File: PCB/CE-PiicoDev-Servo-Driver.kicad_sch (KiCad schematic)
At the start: 33 parts, among them J1 , J2 , J3 Conn_01x03_Male, J4 Conn_01x03_Male, J5 Conn_01x03_Male, J6 Conn_01x02_Male, J7 Conn_01x02_Male, J8 USB_C_Receptacle_USB2.0, J9 USB_C_Receptacle_USB2.0, U1 PCA9685PW

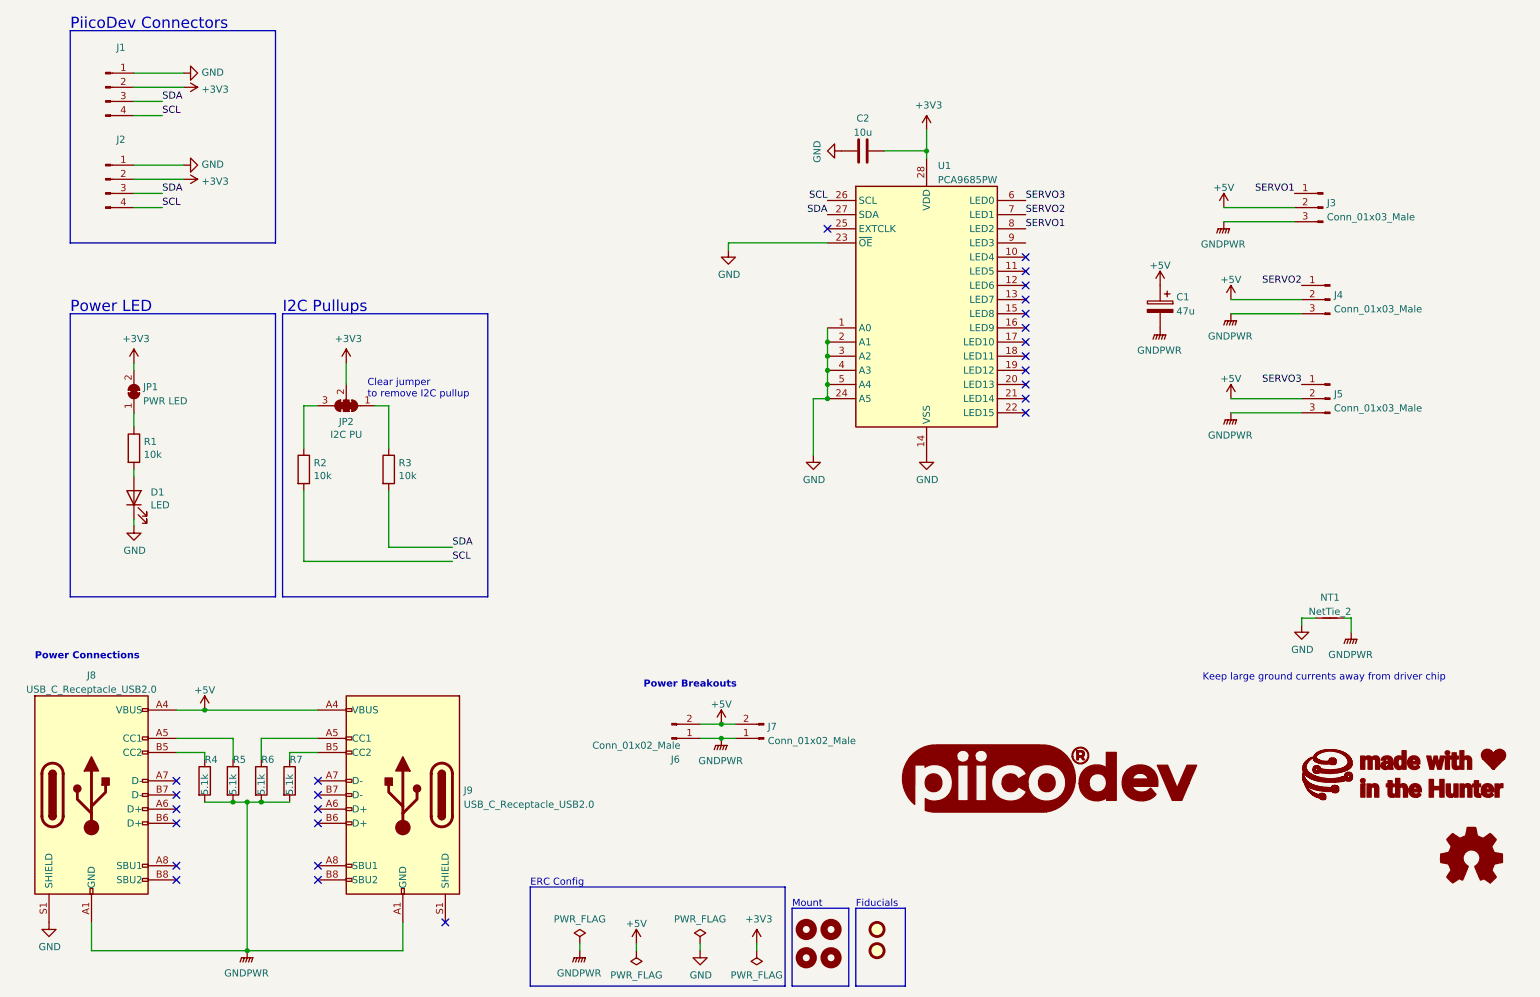
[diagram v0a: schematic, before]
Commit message: include paste on USB connector support tabs
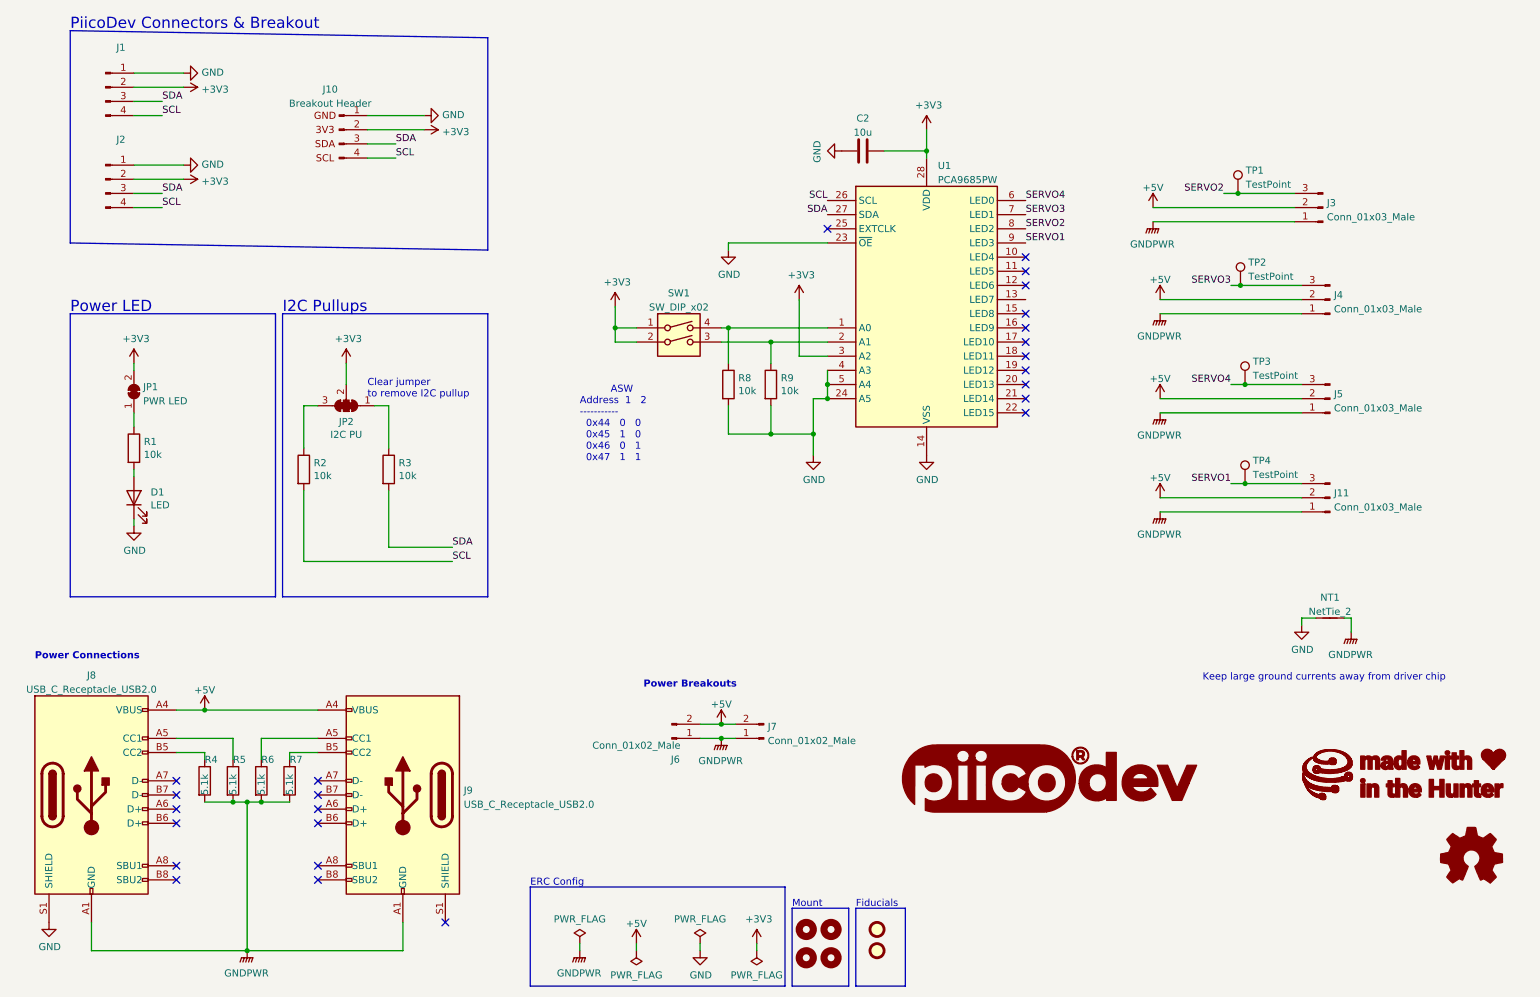
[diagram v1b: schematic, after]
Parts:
- removed C1: 47u, Capacitor_SMD:CP_Elec_6.3x5.3, symbol Device:C_Polarized
- added J10: Breakout Header, CoreElectronics_Components:PiicoDev_header_4pin, symbol CoreElectronics_Components:Conn_PiicoDev_header_01x04_Male
- added J11: Conn_01x03_Male, Connector_PinHeader_2.54mm:PinHeader_1x03_P2.54mm_Vertical_SMD_Pin1Left, symbol Connector:Conn_01x03_Male
- added R8, R9: 10k, Resistor_SMD:R_0402_1005Metric, symbol Device:R
- added SW1: SW_DIP_x02, CoreElectronics_Components:SW_DIP_x02_Slide_CHS-02A1, symbol Switch:SW_DIP_x02
- added TP1, TP2, TP3, TP4: TestPoint, TestPoint:TestPoint_Pad_D1.0mm, symbol Connector:TestPoint
- J3, J4, J5: footprint CoreElectronics_Components:PinHeader_1x03_P2.54mm_Vertical_SMD_Symmetric -> Connector_PinHeader_2.54mm:PinHeader_1x03_P2.54mm_Vertical_SMD_Pin1Left
- J8, J9: footprint Connector_USB:USB_C_Receptacle_HRO_TYPE-C-31-M-12 -> CoreElectronics_Components:USB_C_Receptacle_HRO_TYPE-C-31-M-12-with-paste
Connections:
- net +3V3: now also U1.3 (A2), J10.2 (Pin_2), SW1.1, SW1.2
- net +5V: now also J11.2 (Pin_2)
- net GND: now also J10.1 (Pin_1), R8.2, R9.2; no longer U1.1 (A0), U1.2 (A1), U1.3 (A2)
- net GNDPWR: now also J3.1 (Pin_1), J4.1 (Pin_1), J5.1 (Pin_1), J11.1 (Pin_1); no longer J3.3 (Pin_3), J4.3 (Pin_3), J5.3 (Pin_3)
- net SCL: now also J10.4 (Pin_4)
- net SDA: now also J10.3 (Pin_3)
- net SERVO1: now also U1.9 (LED3), J11.3 (Pin_3), TP4.1; no longer J3.1 (Pin_1), U1.8 (LED2)
- net SERVO2: now also J3.3 (Pin_3), U1.8 (LED2), TP1.1; no longer J4.1 (Pin_1), U1.7 (LED1)
- net SERVO3: now also J4.3 (Pin_3), U1.7 (LED1), TP2.1; no longer J5.1 (Pin_1), U1.6 (LED0)
- new net: R9.1, SW1.3, U1.2 (A1)
- new net: R8.1, SW1.4, U1.1 (A0)
- new net SERVO4: J5.3 (Pin_3), TP3.1, U1.6 (LED0)
- no-connect marks 26 -> 25
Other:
- note added: "ASW Address 1 2 ----------- 0x44 0 0 0x45 1 0 0x46 0 1 0x47 1 1"
- note added: "PiicoDev Connectors & Breakout"
- note removed: "PiicoDev Connectors"
- moved on the sheet: J3, J4, J5

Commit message: v10
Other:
- title: PiicoDev Smart Module 52mm Template -> PiicoDev Servo Driver
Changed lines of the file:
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@@
   (paper "A4")
   (title_block
-    (title "PiicoDev Smart Module 52mm Template")
-    (rev "00")
+    (title "PiicoDev Servo Driver")
+    (date "2022-12-19")
+    (rev "10")
     (company "Core Electronics")
     (comment 1 "Designed by Michael Ruppe at")
